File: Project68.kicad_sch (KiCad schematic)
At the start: 12 parts, among them IC1 MC68008FN, J1 RCJ-044, J2 MD-60S, J3 Micro_SD_Card, J4 Conn_01x03_Pin, U1 PIC18F87K22-xPT, U3 74LS00, U4 74LS74, U5 AMS1117-3.3, Y1 OCXO-14

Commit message: wired I/O ports
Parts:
- added BZ1: Buzzer, symbol Device:Buzzer
- added R1, R2: R, symbol Device:R
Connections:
- net ~{PICDTACK} is gone; now on net ~{BGACK}: U1.27 (RA3/AN3/Vref+)
- net +3.3V: now also J3.4 (VDD)
- net GND: now also J1.1, J2.3, J3.6 (VSS)
- net SD_CLK: now also J3.5 (CLK)
- net SD_CS: now also J3.2 (DAT3/CD)
- net SD_IN: now also J3.7 (DAT0)
- net SD_OUT: now also J3.3 (CMD)
- net VCC: now also J2.4
- net VIDPIXEL: now also R1.1
- net VIDSYNC: now also R2.1
- net ~{BGACK}: no longer U1.50 (RA6/OSC2)
- net at J1.2: now also R1.2, R2.2
- net PS2_DATA: now reaches J2.1
- net PS2_CLK: now reaches J2.5
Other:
- moved on the sheet: J1, J3

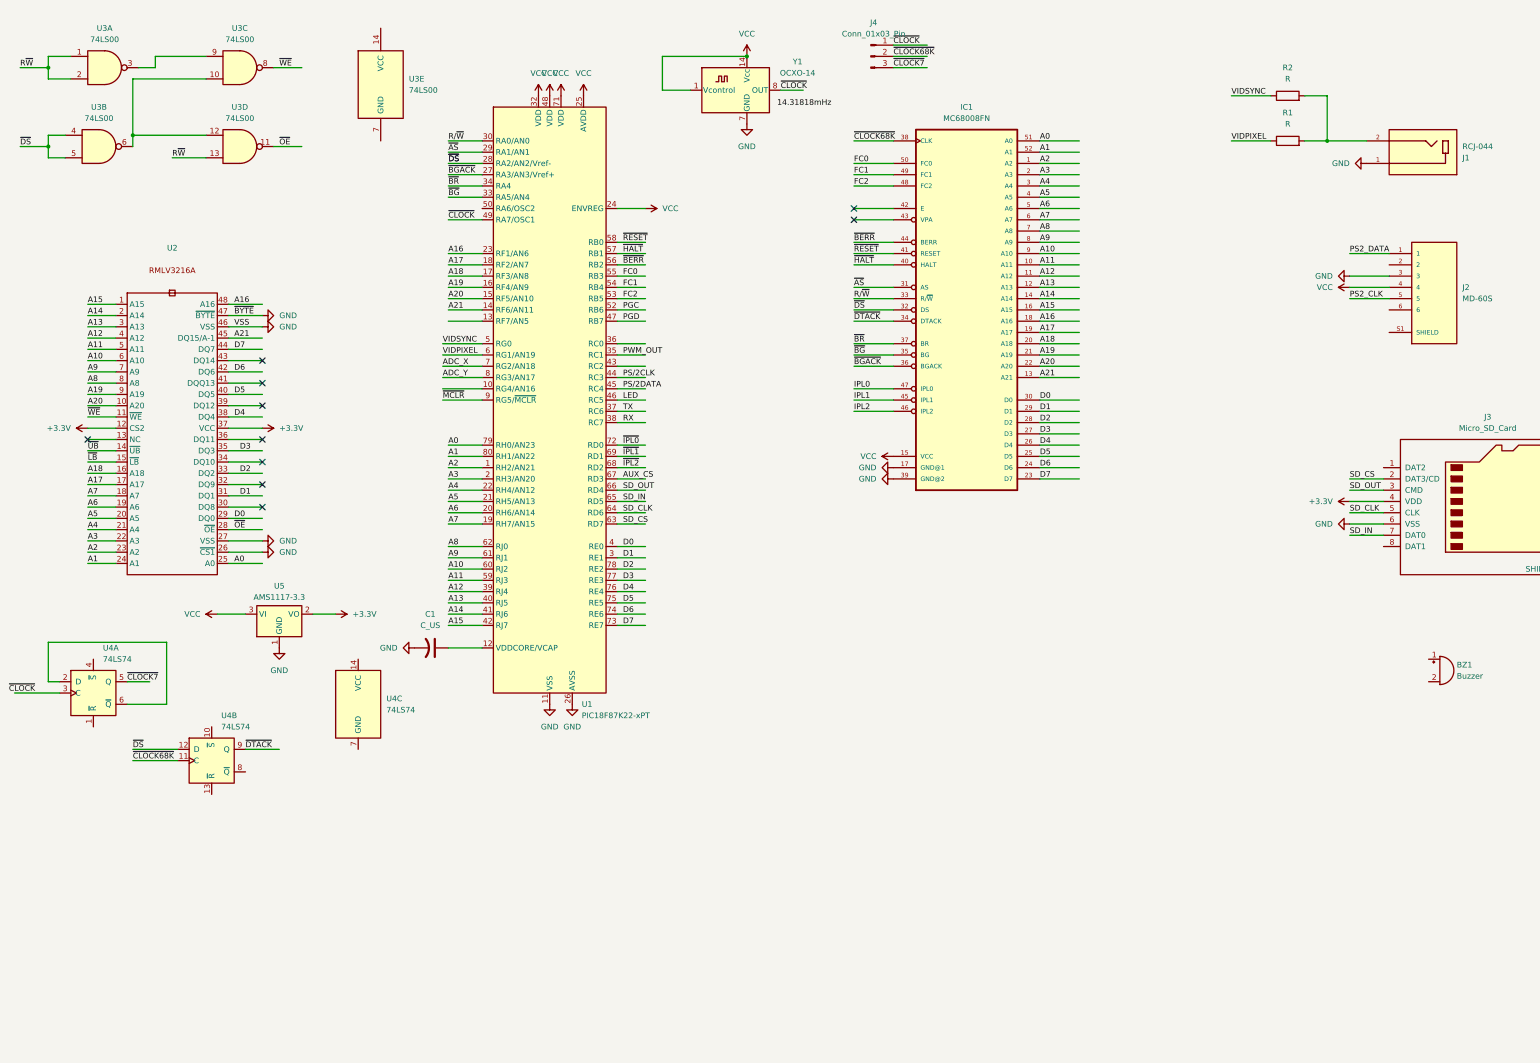
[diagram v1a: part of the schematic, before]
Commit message: added status LED
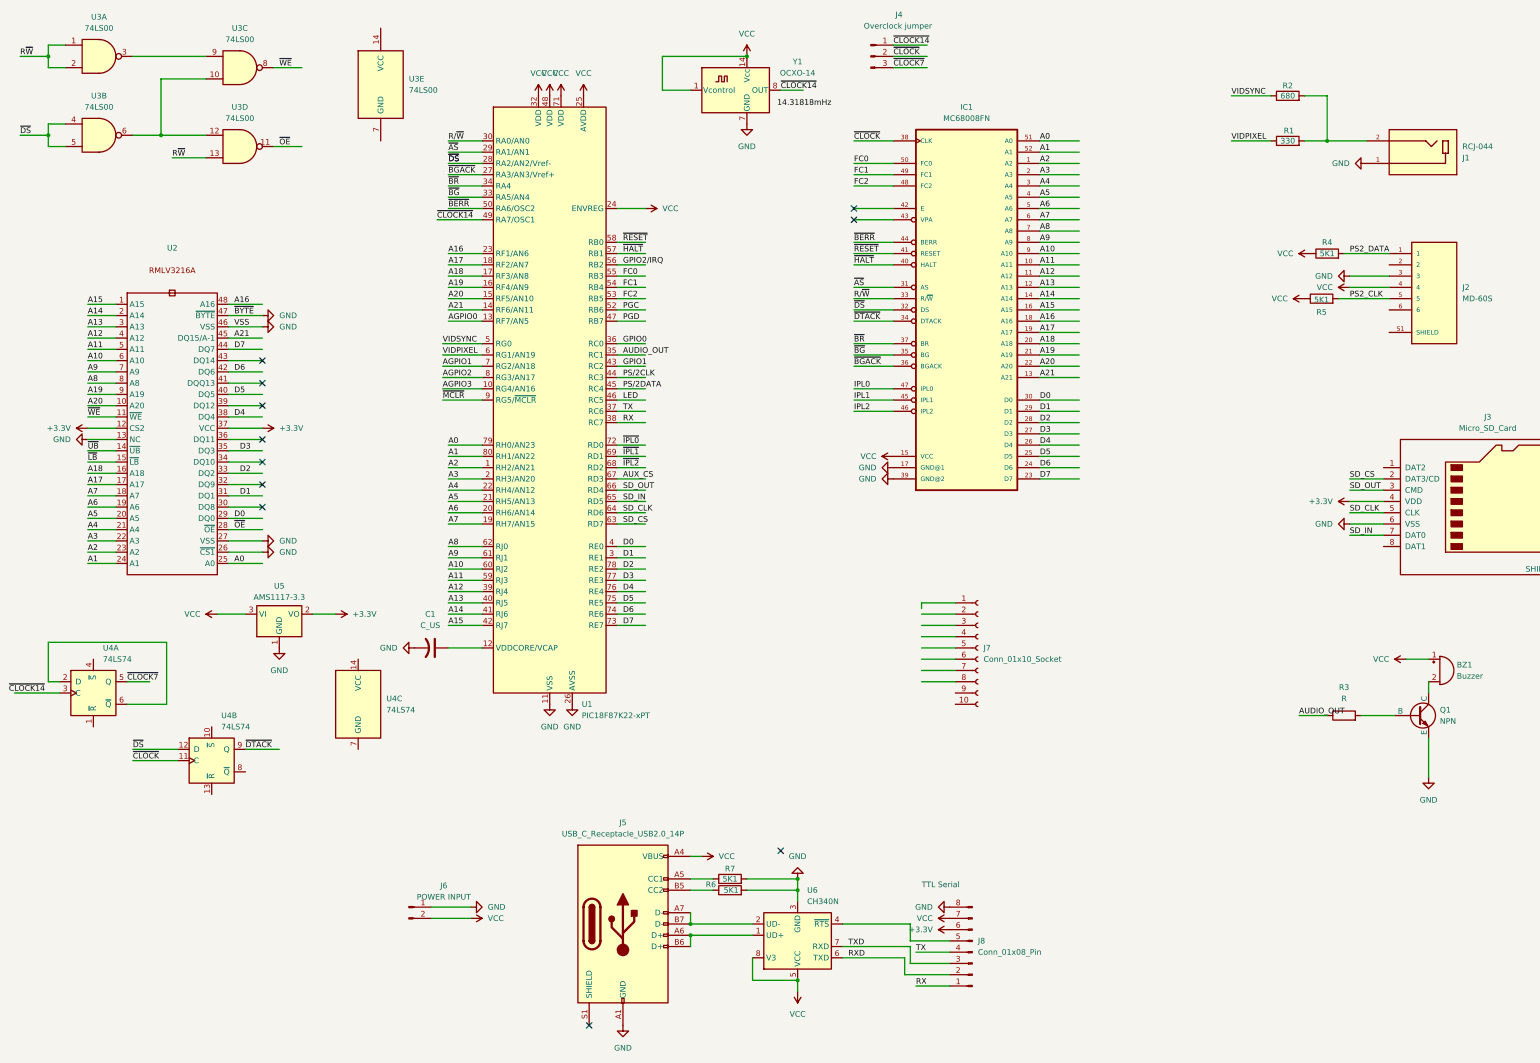
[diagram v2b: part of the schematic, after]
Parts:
- added J5: USB_C_Receptacle_USB2.0_14P, symbol Connector:USB_C_Receptacle_USB2.0_14P
- added J6: POWER INPUT, Connector_PinHeader_2.54mm:PinHeader_1x02_P2.54mm_Vertical, symbol Connector:Conn_01x02_Pin
- added J7: Conn_01x10_Socket, symbol Connector:Conn_01x10_Socket
- added J8: Conn_01x08_Pin, symbol Connector:Conn_01x08_Pin
- added Q1: NPN, symbol Simulation_SPICE:NPN
- added R3: R, symbol Device:R
- added R4, R5, R6, R7: 5K1, symbol Device:R
- added U6: CH340N, Package_SO:SOP-8_3.9x4.9mm_P1.27mm, symbol Interface_USB:CH340N
- J4: value Conn_01x03_Pin -> Overclock jumper
- R1: value R -> 330
- R2: value R -> 680
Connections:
- net ~{CLOCK68K} is gone; now on net ~{CLOCK}: IC1.38 (CLK), J4.2 (Pin_2), U4.11 (C)
- net +3.3V: now also J8.6 (Pin_6)
- net GND: now also U2.13 (NC), J5.A1 (GND), J5.A12 (GND), J5.B1 (GND), J5.B12 (GND), J6.1 (Pin_1), J8.8 (Pin_8), Q1.3 (E), R6.2, R7.2, U6.3 (GND)
- net PS2_CLK: now also R5.2
- net PS2_DATA: now also R4.2
- net RX: now also J8.1 (Pin_1)
- net TX: now also J8.4 (Pin_4)
- net VCC: now also BZ1.1 (+), J5.A4 (VBUS), J5.A9 (VBUS), J5.B4 (VBUS), J5.B9 (VBUS), J6.2 (Pin_2), J8.7 (Pin_7), R4.1, R5.1, U6.5 (VCC), U6.8 (V3)
- net ~{BERR}: now also U1.50 (RA6/OSC2); no longer U1.56 (RB2)
- net ~{CLOCK}: no longer J4.1 (Pin_1), U1.49 (RA7/OSC1), Y1.8 (OUT)
- net AGPIO3: now reaches U1.10 (RG4/AN16)
- net AGPIO0: now reaches U1.13 (RF7/AN5)
- net GPIO0: now reaches U1.36 (RC0)
- net GPIO1: now reaches U1.43 (RC2)
- net at BZ1.2 (-): now also Q1.1 (C)
- net ADC_X renamed AGPIO1
- net ADC_Y renamed AGPIO2
- net PWM_OUT renamed AUDIO_OUT
- net AUDIO_OUT: now also R3.1
- new net: J5.A5 (CC1), R7.1
- new net: J5.A6 (D+), J5.B6 (D+), U6.1 (UD+)
- new net: J5.A7 (D-), J5.B7 (D-), U6.2 (UD-)
- new net: J5.B5 (CC2), R6.1
- new net: J8.5 (Pin_5), U6.4 (~{RTS})
- new net: Q1.2 (B), R3.2
- new net GPIO2/IRQ: U1.56 (RB2)
- new net RXD: J8.2 (Pin_2), U6.6 (TXD)
- new net TXD: J8.3 (Pin_3), U6.7 (RXD)
- new net ~{CLOCK14}: J4.1 (Pin_1), U1.49 (RA7/OSC1), Y1.8 (OUT)
- no-connect marks 10 -> 11
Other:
- note added: "TTL Serial"
- moved on the sheet: U3A, U3B

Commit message: level shifters & CH340
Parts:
- added D1: LED, symbol Device:LED
- added R8: 220, symbol Device:R
- added R9: R, symbol Device:R
- added U10, U7, U8, U9: TXS0108EPW, Package_SO:TSSOP-20_4.4x6.5mm_P0.65mm, symbol Logic_LevelTranslator:TXS0108EPW
- added U11: PIC18F87J11T-I_PT, PIC18F87J11T-I_PT:QFP50P1400X1400X120-80N, symbol PIC18F87J11T-I_PT:PIC18F87J11T-I_PT
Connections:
- net +3.3V: now also R9.1, U10.2 (VCCA), U7.2 (VCCA), U8.2 (VCCA), U9.2 (VCCA)
- net A0: now also U7.20 (B1); no longer U2.25 (A0)
- net A1: now also U7.18 (B2)
- net A10: now also U8.17 (B3); no longer U2.6 (A10)
- net A11: now also U8.16 (B4); no longer U2.5 (A11)
- net A12: now also U8.15 (B5); no longer U2.4 (A12)
- net A13: now also U8.14 (B6); no longer U2.3 (A13)
- net A14: now also U8.13 (B7); no longer U2.2 (A14)
- net A15: now also U8.12 (B8); no longer U2.1 (A15)
- net A16: now also U9.20 (B1); no longer U2.48 (A16)
- net A17: now also U9.18 (B2)
- net A18: now also U9.17 (B3)
- net A19: now also U9.16 (B4); no longer U2.9 (A19)
- net A2: now also U7.17 (B3)
- net A20: now also U9.15 (B5); no longer U2.10 (A20)
- net A21: now also U9.14 (B6); no longer U2.45 (DQ15/A-1)
- net A3: now also U7.16 (B4)
- net A4: now also U7.15 (B5)
- net A5: now also U7.14 (B6)
- net A6: now also U7.13 (B7)
- net A7: now also U7.12 (B8)
- net A8: now also U8.20 (B1); no longer U2.8 (A8)
- net A9: now also U8.18 (B2); no longer U2.7 (A9)
- net D0: now also U10.20 (B1); no longer U2.29 (DQ0)
- net D1: now also U10.18 (B2); no longer U2.31 (DQ1)
- net D2: now also U10.17 (B3); no longer U2.33 (DQ2)
- net D3: now also U10.16 (B4); no longer U2.35 (DQ3)
- net D4: now also U10.15 (B5); no longer U2.38 (DQ4)
- net D5: now also U10.14 (B6); no longer U2.40 (DQ5)
- net D6: now also U10.13 (B7); no longer U2.42 (DQ6)
- net D7: now also U10.12 (B8); no longer U2.44 (DQ7)
- net GND: now also R8.2, U10.11 (GND), U7.11 (GND), U8.11 (GND), U9.11 (GND)
- net LED: now also D1.2 (A)
- net VCC: now also U10.19 (VCCB), U7.19 (VCCB), U8.19 (VCCB), U9.19 (VCCB)
- net ~{OE}: now also U9.12 (B8); no longer U2.28 (~{OE})
- net ~{WE}: now also U9.13 (B7); no longer U2.11 (~{WE})
- new net: U11.11 (VSS), U11.31 (VSS), U11.51 (VSS), U11.70 (VSS)
- new net: U11.32 (VDD), U11.48 (VDD), U11.71 (VDD)
- new net: D1.1 (K), R8.1
- new net AA0: U2.25 (A0), U7.1 (A1)
- new net AA1: U7.3 (A2)
- new net AA10: U2.6 (A10), U8.4 (A3)
- new net AA11: U2.5 (A11), U8.5 (A4)
- new net AA12: U2.4 (A12), U8.6 (A5)
- new net AA13: U2.3 (A13), U8.7 (A6)
- new net AA14: U2.2 (A14), U8.8 (A7)
- new net AA15: U2.1 (A15), U8.9 (A8)
- new net AA16: U2.48 (A16), U9.1 (A1)
- new net AA17: U9.3 (A2)
- new net AA18: U9.4 (A3)
- new net AA19: U2.9 (A19), U9.5 (A4)
- new net AA2: U7.4 (A3)
- new net AA20: U2.10 (A20), U9.6 (A5)
- new net AA21: U2.45 (DQ15/A-1), U9.7 (A6)
- new net AA3: U7.5 (A4)
- new net AA4: U7.6 (A5)
- new net AA5: U7.7 (A6)
- new net AA6: U7.8 (A7)
- new net AA7: U7.9 (A8)
- new net AA8: U2.8 (A8), U8.1 (A1)
- new net AA9: U2.7 (A9), U8.3 (A2)
- new net DD0: U10.1 (A1), U2.29 (DQ0)
- new net DD1: U10.3 (A2), U2.31 (DQ1)
- new net DD2: U10.4 (A3), U2.33 (DQ2)
- new net DD3: U10.5 (A4), U2.35 (DQ3)
- new net DD4: U10.6 (A5), U2.38 (DQ4)
- new net DD5: U10.7 (A6), U2.40 (DQ5)
- new net DD6: U10.8 (A7), U2.42 (DQ6)
- new net DD7: U10.9 (A8), U2.44 (DQ7)
- new net OE: R9.2, U10.10 (OE), U7.10 (OE), U8.10 (OE), U9.10 (OE)
- new net ~{OOE}: U2.28 (~{OE}), U9.9 (A8)
- new net ~{WWE}: U2.11 (~{WE}), U9.8 (A7)
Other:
- moved on the sheet: J5, J6, J8, R6, R7, U6
